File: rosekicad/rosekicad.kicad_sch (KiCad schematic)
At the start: 0 parts

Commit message: first upload test
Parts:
- added A1: Arduino_UNO_R3, Module:Arduino_UNO_R3, symbol MCU_Module:Arduino_UNO_R3
- added C1: 470 uF, symbol Device:C_Polarized
- added Q1: 2N2222, Package_TO_SOT_THT:TO-92_Inline, symbol Transistor_BJT:2N3904
- added R1: 220, symbol Device:R
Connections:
- new net: C1.1, Q1.2 (B), R1.1
- new net GND: C1.2

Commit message: updated scheatic
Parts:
- added C1 (x2): 470 uF, symbol Device:C_Polarized
- added D1 (x9): 1N4148, Diode_THT:D_DO-35_SOD27_P7.62mm_Horizontal, symbol Diode:1N4148
- added J1 (x12): Solenoid, symbol Connector:Screw_Terminal_01x02
- added J2: UV Lights, symbol Connector:Screw_Terminal_01x02
- added J3: LED Lights, symbol Connector:Screw_Terminal_01x02
- added J4: Barrel_Jack_MountingPin, symbol Connector:Barrel_Jack_MountingPin
- added J5: DMX Cable, symbol Connector:Screw_Terminal_01x05
- added Q1 (x14): 2N2222, Package_TO_SOT_THT:TO-92_Inline, symbol Transistor_BJT:2N3904
- added R1 (x2): 220, symbol Device:R
- added R2 (x12): 2.2, symbol Device:R
- added R3 (x12): 100, symbol Device:R
- added U1: MAX485E, Package_SO:SOIC-8_3.9x4.9mm_P1.27mm, symbol Interface_UART:MAX485E
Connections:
- net GND: now also A1.29 (GND), A1.6 (GND), A1.7 (GND), C1.2, C1.2, J2.2 (Pin_2), J3.2 (Pin_2), J4.2, J5.1 (Pin_1), Q1.1 (E), Q1.1 (E), Q1.1 (E), Q1.1 (E), Q1.1 (E), Q1.1 (E), Q1.1 (E), Q1.1 (E), Q1.1 (E), Q1.1 (E), Q1.1 (E), Q1.1 (E), U1.2 (~{RE}), U1.3 (DE), U1.5 (GND)
- net at Q1.1 (E): now also D1.1 (K), R3.2
- net +5V: now reaches Q1.3 (C)
- net +5V: now also J4.1, Q1.3 (C), Q1.3 (C), R2.1, R2.1, R2.1, R2.1, R2.1, R2.1, R2.1, R2.1, R2.1, R2.1, R2.1, R2.1
- net at R1.2: now also A1.21 (D6)
- net at A1.15 (D0/RX): now also U1.1 (RO)
- net at A1.16 (D1/TX): now also U1.4 (DI)
- net at A1.18 (D3): now also J2.1 (Pin_1)
- net at A1.20 (D5): now also J3.1 (Pin_1)
- net at A1.24 (D9): now also R1.2
- net at A1.26 (D11): now also R1.2
- net at A1.5 (+5V): now also U1.8 (VCC)
- new net: J1.1 (Pin_1), R2.2 (x12)
- new net: Q1.2 (B), R3.1 (x12)
- new net: D1.1 (K), D1.2 (A), R3.2 (x6)
- new net: D1.1 (K), Q1.1 (E), R3.2 (x2)
- new net: D1.2 (A), R3.2 (x3)
- new net: J1.2 (Pin_2), Q1.3 (C) (x12)
- new net: C1.1, Q1.2 (B), R1.1 (x2)
- new net: J5.2 (Pin_2), U1.6 (A)
- new net: J5.3 (Pin_3), U1.7 (B)
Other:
- company: (none) -> Anna Tretiakova
- title: (none) -> Senior Design Rose
- moved on the sheet: C1, Q1, R1

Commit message: updated scheatic
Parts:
- D1: footprint Diode_THT:D_DO-35_SOD27_P7.62mm_Horizontal -> Diode_THT:D_DO-35_SOD27_P10.16mm_Horizontal
- renumbered C1 to C2, C1 to C3, D1 to D2, D1 to D3, D1 to D4, D1 to D5, D1 to D6, D1 to D7, D1 to D8, D1 to D9, J1 to J10, J1 to J11, J1 to J12, J2 to J13, J3 to J14, J5 to J15, J4 to J16, J1 to J2, J1 to J3, J1 to J4, J1 to J5, J1 to J6, J1 to J7, J1 to J8, J1 to J9, Q1 to Q10, Q1 to Q11, Q1 to Q12, Q1 to Q13, Q1 to Q14, Q1 to Q15, Q1 to Q2, Q1 to Q3, Q1 to Q4, Q1 to Q5, Q1 to Q6, Q1 to Q7, Q1 to Q8, Q1 to Q9, R1 to R10, R2 to R11, R2 to R12, R2 to R13, R2 to R14, R3 to R15, R3 to R16, R3 to R17, R3 to R18, R1 to R19, R2 to R20, R2 to R21, R2 to R22, R2 to R23, R3 to R24, R3 to R25, R3 to R26, R3 to R27, R2 to R3, R2 to R4, R2 to R5, R3 to R6, R3 to R7, R3 to R8, R3 to R9

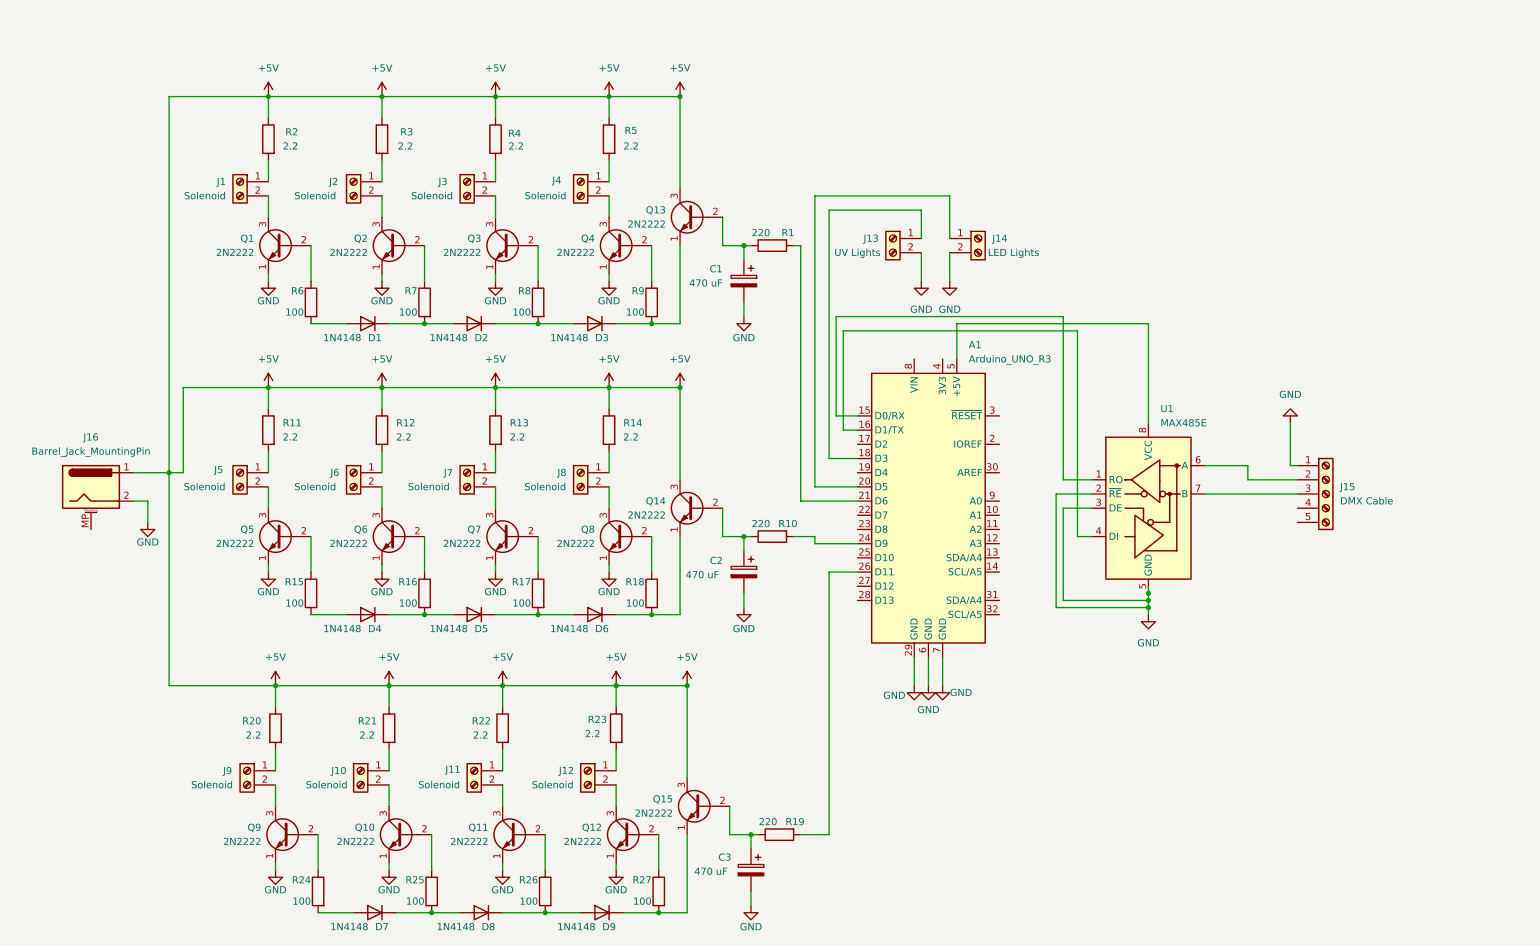
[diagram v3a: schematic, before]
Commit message: updated footprints
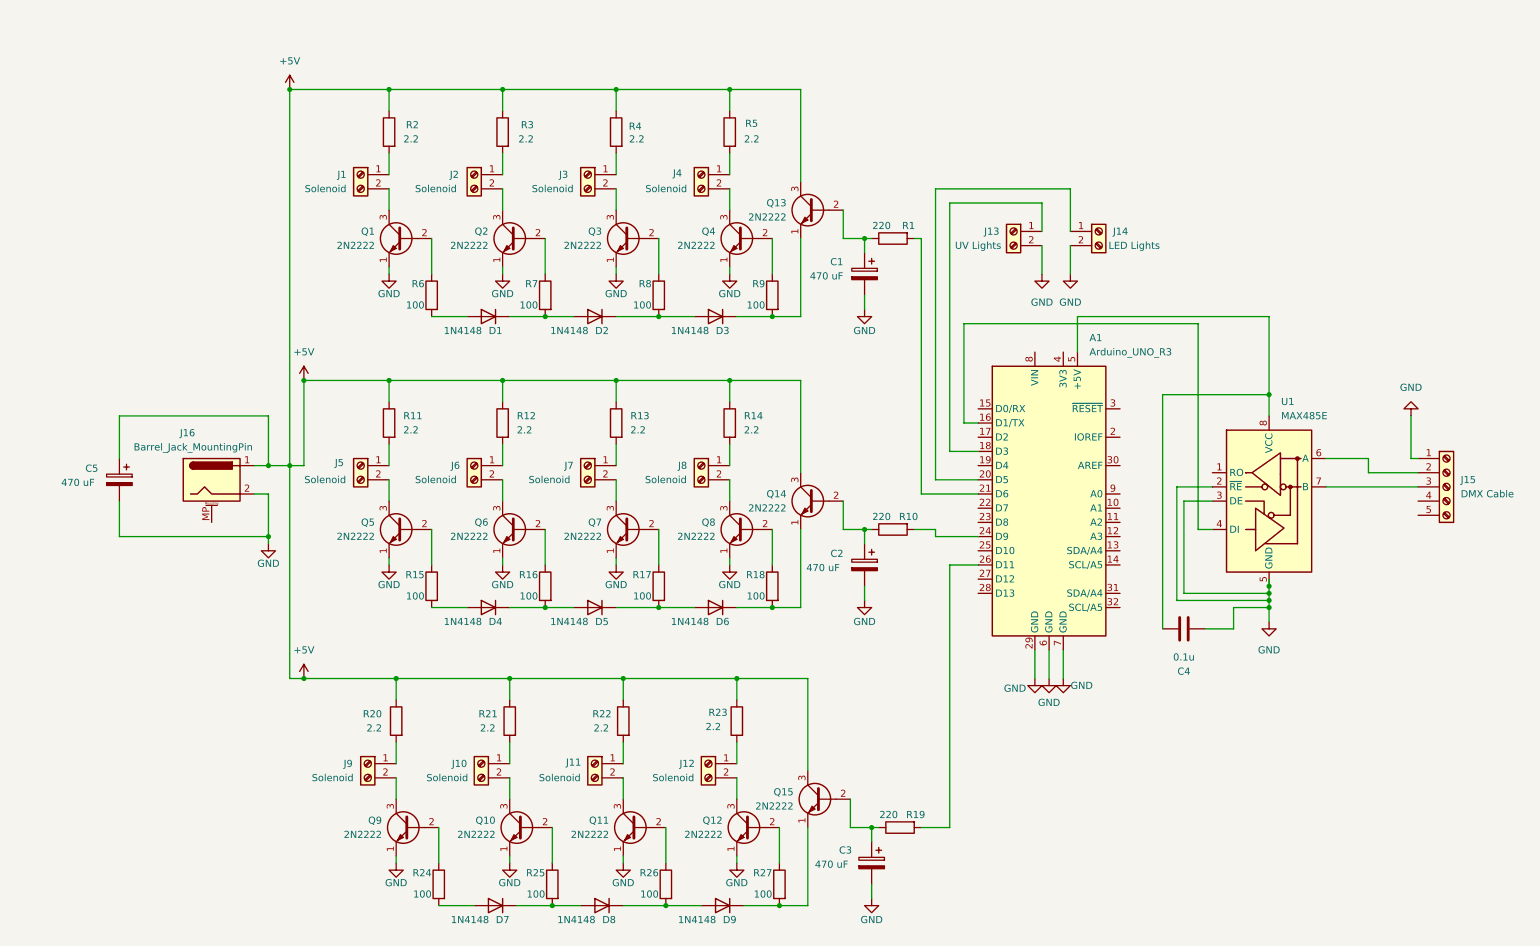
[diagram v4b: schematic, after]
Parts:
- added C4: 0.1u, Capacitor_THT:CP_Radial_D5.0mm_P2.00mm, symbol Device:C
- added C5: 470 uF, Capacitor_THT:CP_Radial_D10.0mm_P3.80mm, symbol Device:C_Polarized
- C1, C2, C3: footprint (none) -> Capacitor_THT:CP_Radial_D10.0mm_P3.80mm
- J1, J10, J11, J12, J13, J14, J2, J3, J4, J5, J6, J7, J8, J9: footprint (none) -> TerminalBlock:TerminalBlock_MaiXu_MX126-5.0-02P_1x02_P5.00mm
- J15: footprint (none) -> TerminalBlock:TerminalBlock_MaiXu_MX126-5.0-05P_1x05_P5.00mm
- J16: footprint (none) -> Connector_BarrelJack:BarrelJack_CUI_PJ-102AH_Horizontal
- R1, R10, R11, R12, R13, R14, R15, R16, R17, R18, R19, R2, R20, R21, R22, R23, R24, R25, R26, R27, R3, R4, R5, R6, R7, R8, R9: footprint (none) -> Resistor_THT:R_Axial_DIN0207_L6.3mm_D2.5mm_P7.62mm_Horizontal
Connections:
- net +5V: now also C5.1
- net GND: now also C4.2, C5.2
- net at A1.15 (D0/RX): no longer U1.1 (RO)
- net at A1.5 (+5V), U1.8 (VCC): now also C4.1
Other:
- moved on the sheet: A1, C1, C2, C3, D1, D2, D3, D4, D5, D6, D7, D8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

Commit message: pcd built
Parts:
- D1: footprint Diode_THT:D_DO-35_SOD27_P10.16mm_Horizontal -> Diode_THT:D_DO-35_SOD27_P7.62mm_Horizontal
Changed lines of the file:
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@@
 			)
 		)
-		(property "Footprint" "Diode_THT:D_DO-35_SOD27_P10.16mm_Horizontal"
+		(property "Footprint" "Diode_THT:D_DO-35_SOD27_P7.62mm_Horizontal"
 			(at 95.25 68.58 0)
 			(effects

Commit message: added footprint
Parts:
- U1: footprint Package_SO:SOIC-8_3.9x4.9mm_P1.27mm -> (none)
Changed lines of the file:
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@@
 			)
 		)
-		(property "Footprint" "Package_SO:SOIC-8_3.9x4.9mm_P1.27mm"
+		(property "Footprint" ""
 			(at 234.95 124.46 0)
 			(effects

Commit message: updated pcb
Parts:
- U1: footprint (none) -> rosekicad:MAX485_Module
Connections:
- net at Q13.1 (E), R9.2: now also D3.2 (A); no longer D3.1 (K)
- net at Q15.1 (E), R27.2: now also D9.2 (A); no longer D9.1 (K)
- net at D4.2 (A): now also D5.1 (K), R16.2; no longer R15.2
- net at D7.2 (A): now also D8.1 (K), R25.2; no longer R24.2
- net at Q14.1 (E), R18.2: now also D6.2 (A); no longer D6.1 (K)
- net at D1.2 (A): now also D2.1 (K), R7.2; no longer R6.2
- new net: D8.2 (A), D9.1 (K), R26.2
- new net: D4.1 (K), R15.2
- new net: D5.2 (A), D6.1 (K), R17.2
- new net: D2.2 (A), D3.1 (K), R8.2
- new net: D7.1 (K), R24.2
- new net: D1.1 (K), R6.2
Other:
- moved on the sheet: A1, C1, C2, C3, C4, C5, D1, D2, D3, D4, D5, D6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

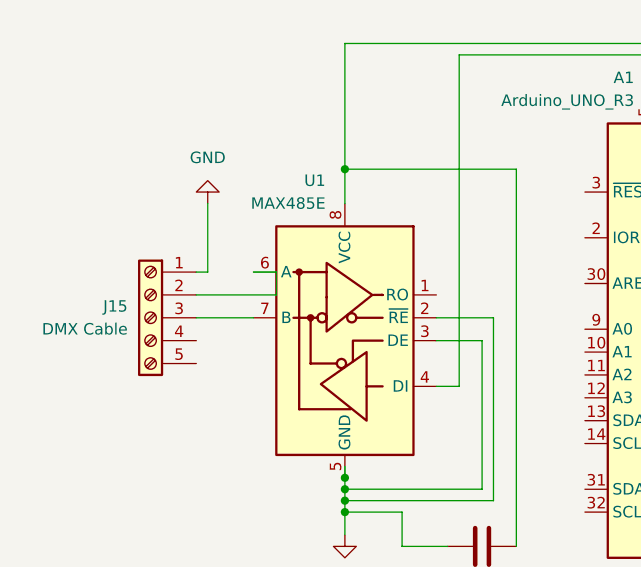
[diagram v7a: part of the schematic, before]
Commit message: Added four layers
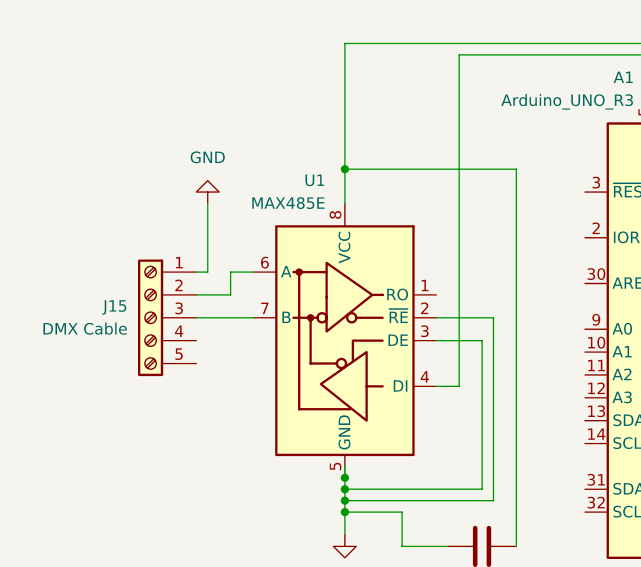
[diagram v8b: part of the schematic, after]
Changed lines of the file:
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@@
-	(wire
-		(pts
-			(xy 41.91 86.36) (xy 39.37 86.36)
-		)
-		(stroke
-			(width 0)
-			(type default)
-		)
-	)
 	(wire
 		(pts
@@
 	(wire
 		(pts
-			(xy 33.02 88.9) (xy 41.91 88.9)
-		)
-		(stroke
-			(width 0)
-			(type default)
-		)
-	)
-	(wire
-		(pts
 			(xy 68.58 74.93) (xy 68.58 116.84)
 		)
@@
 	(wire
 		(pts
+			(xy 39.37 86.36) (xy 36.83 86.36)
+		)
+		(stroke
+			(width 0)
+			(type default)
+		)
+	)
+	(wire
+		(pts
 			(xy 125.73 41.91) (xy 125.73 46.99)
 		)
@@
 	(wire
 		(pts
+			(xy 36.83 88.9) (xy 33.02 88.9)
+		)
+		(stroke
+			(width 0)
+			(type default)
+		)
+	)
+	(wire
+		(pts
 			(xy 222.25 125.73) (xy 205.74 125.73)
 		)
@@
 	(wire
 		(pts
+			(xy 36.83 86.36) (xy 36.83 88.9)
+		)
+		(stroke
+			(width 0)
+			(type default)
+		)
+	)
+	(wire
+		(pts
 			(xy 101.6 90.17) (xy 109.22 90.17)
 		)
@@
 		)
 		(stroke
-			(width 0)
-			(type default)
-		)
-	)
-	(wire
-		(pts
-			(xy 41.91 88.9) (xy 41.91 86.36)
-		)
-		(stroke
